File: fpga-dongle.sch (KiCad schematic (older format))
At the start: 109 parts, among them P1 USB_PWR, P2 PGM, P3 right, P4 left, P5 CONN_01X40, P6 CONN_01X40, P7 DBG_SWD, P8 USB_PWR, Q1 BC857, SW1 T1107A(6x3,8x2,5MM)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

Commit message: Add miltiple power source handling, reroute pertinent nets
Signed-off-by: Martin Ribelotta <martinribelotta@gmail.com>
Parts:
- added D10, D4, D5, D6, D7, D8, D9: 1N5819(S4SOD-123), Diodes_SMD:SOD-123, symbol D_Schottky
- added R42, R43, R44: 10k, Resistors_SMD:R_0805, symbol R
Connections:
- net +3V3: now also C3.2, U3.1 (Vin), U3.3 (EN), D4.1 (K), D5.1 (K), D6.1 (K); no longer C8.2, L1.2, P3.1 (P1), P4.1 (P1), U2.4 (Vout)
- net +5V: now also D10.1 (K), D7.1 (K), D8.1 (K), D9.1 (K); no longer C3.2, C5.2, C7.2, D1.1, F1.2, F2.2, U3.1 (Vin), U3.3 (EN)
- net GND: now also R44.1
- net CIAA_5V2: now reaches P3.2 (P2)
- net CIAA_5V2: now also D8.2 (A), R42.2
- net CIAA_5V1: now reaches P4.2 (P2)
- net CIAA_5V1: now also D7.2 (A)
- net at U6.45 (PIO0_17/CT32B0_C0/SCLK): now also R42.1, R43.1
- new net: C5.2, C7.2, D1.1, D9.2 (A), F1.2
- new net: C8.2, D4.2 (A), L1.2, U2.4 (Vout)
- new net: D10.2 (A), F2.2
- new net: R43.2, R44.2
- new net CIAA_3V3_1: D6.2 (A), P4.1 (P1)
- new net CIAA_3V3_2: D5.2 (A), P3.1 (P1)
- no-connect marks 39 -> 36
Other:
- moved on the sheet: PWRLED1, R9

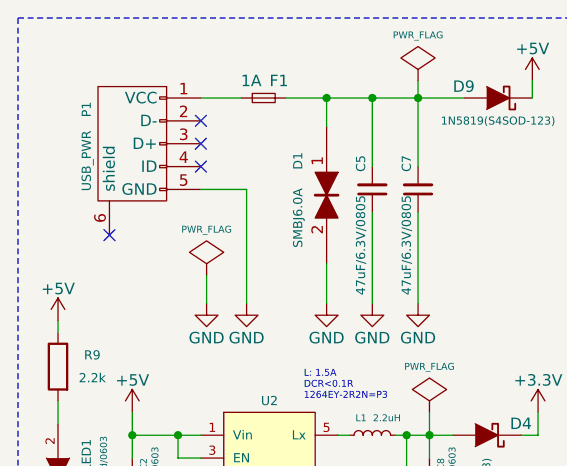
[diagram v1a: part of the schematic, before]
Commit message: Change USB power-only connector by screw connector
Signed-off-by: Martin Ribelotta <martinribelotta@gmail.com>
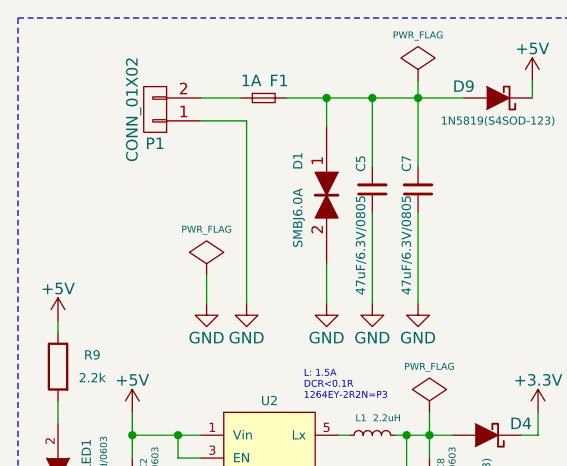
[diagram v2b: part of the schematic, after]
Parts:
- removed P1: USB_PWR, OLIMEX_Connectors-FP:USB_Mini-B-NOSILK, symbol USB_OTG
- added P1: CONN_01X02, Connect:AK300-2, symbol CONN_01X02
- D3: footprint LEDs:LED_0603 -> LEDs:LED_0805
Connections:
- net GND: now also P1.1 (P1)
- net at F1.1: now also P1.2 (P2)
- no-connect marks 36 -> 32
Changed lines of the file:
@@
 $EndComp
-$Comp
-L USB_OTG P1
-U 1 1 57D6B02D
-P 1450 1325
-F 0 "P1" H 1300 1525 40  0000 C CNN
-F 1 "USB_PWR" H 1525 1525 40  0000 C CNN
-F 2 "OLIMEX_Connectors-FP:USB_Mini-B-NOSILK" V 1400 1225 50  0001 C CNN
-F 3 "" V 1400 1225 50  0000 C CNN
-	1    1450 1325
-	0    -1   1    0
-$EndComp
-NoConn ~ 1350 1725
-NoConn ~ 1750 1425
 $Comp
 L TVS D1
@@
 F 0 "D3" H 11200 12575 50  0000 C CNN
 F 1 "LED" H 11200 12375 50  0000 C CNN
-F 2 "LEDs:LED_0603" H 11200 12475 50  0001 C CNN
+F 2 "LEDs:LED_0805" H 11200 12475 50  0001 C CNN
 F 3 "" H 11200 12475 50  0000 C CNN
 	1    11200 12475
@@
 Text Label 12225 13275 2    60   ~ 0
 USB_N
-NoConn ~ 1750 1225
-NoConn ~ 1750 1325
 Text Label 9850 13525 0    60   ~ 0
 D_USB_N
@@
 	1750 1125 1925 1125
 Wire Wire Line
-	1750 1525 1950 1525
-Wire Wire Line
-	1950 1525 1950 2025
+	1750 1225 1950 1225
+Wire Wire Line
+	1950 1225 1950 2025
 Wire Wire Line
 	2300 1250 2300 1125
@@
 Wire Wire Line
 	1125 2100 1125 2150
+$Comp
+L CONN_01X02 P1
+U 1 1 57F72785
+P 1550 1175
+F 0 "P1" H 1550 1325 50  0000 C CNN
+F 1 "CONN_01X02" V 1650 1175 50  0000 C CNN
+F 2 "Connect:AK300-2" H 1550 1175 50  0001 C CNN
+F 3 "" H 1550 1175 50  0000 C CNN
+	1    1550 1175
+	-1   0    0    1
+$EndComp
 $EndSCHEMATC

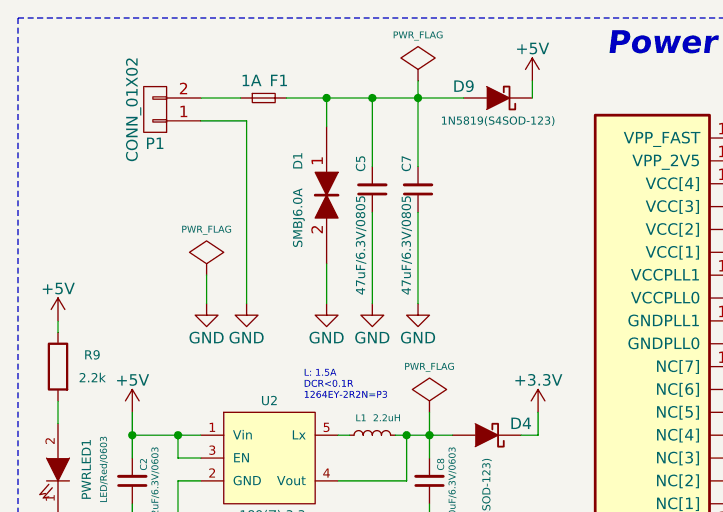
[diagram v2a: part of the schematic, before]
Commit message: Partial rework of changes lost in last conflict
Signed-off-by: Martin Ribelotta <martinribelotta@gmail.com>
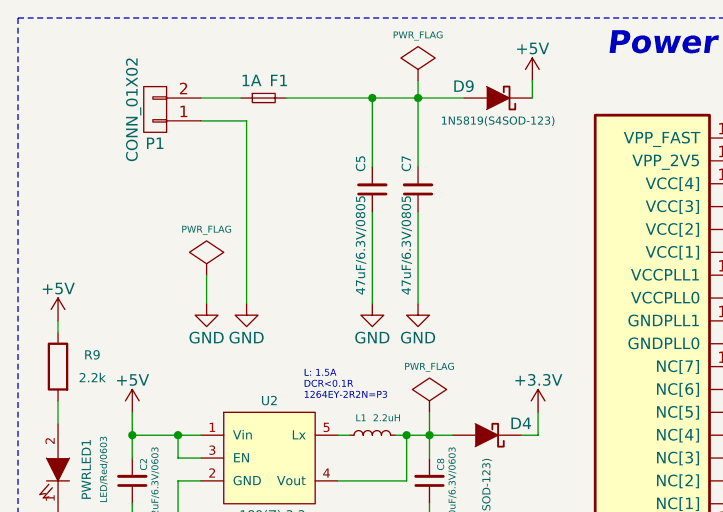
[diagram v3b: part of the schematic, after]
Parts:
- removed D1: SMBJ6.0A, Diodes_SMD:DO-214AB, symbol TVS
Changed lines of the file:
@@
 Power Supply
 $Comp
-L GND #PWR01
-U 1 1 579395D3
-P 2300 2025
-F 0 "#PWR01" H 2300 1775 50  0001 C CNN
-F 1 "GND" H 2300 1875 50  0000 C CNN
-F 2 "" H 2300 2025 60  0000 C CNN
-F 3 "" H 2300 2025 60  0000 C CNN
-	1    2300 2025
-	-1   0    0    -1
-$EndComp
-$Comp
 L C_Small C5
 U 1 1 579395D5
@@
 $EndComp
 $Comp
-L TVS D1
-U 1 1 57D6C6A1
-P 2300 1550
-F 0 "D1" H 2150 1425 40  0000 C CNN
-F 1 "SMBJ6.0A" H 2400 1425 40  0000 C CNN
-F 2 "Diodes_SMD:DO-214AB" H 2300 1550 50  0001 C CNN
-F 3 "" H 2300 1550 50  0000 C CNN
-	1    2300 1550
-	0    1    1    0
-$EndComp
-$Comp
 L L_Small L2
 U 1 1 57D707DC
@@
 	1950 1225 1950 2025
 Wire Wire Line
-	2300 1250 2300 1125
-Connection ~ 2300 1125
-Wire Wire Line
-	2300 2025 2300 1850
-Wire Wire Line
 	2950 3575 2950 3475

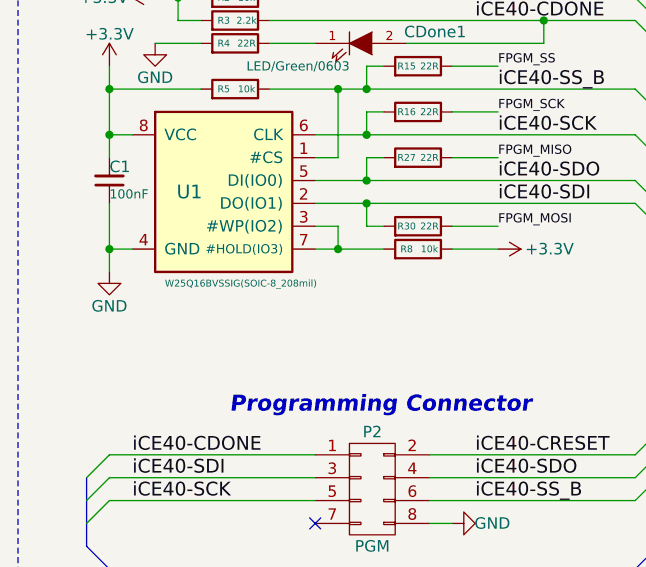
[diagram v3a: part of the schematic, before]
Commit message: More PCB annotations, some rework on GND plane
Signed-off-by: Martin Ribelotta <martinribelotta@gmail.com>
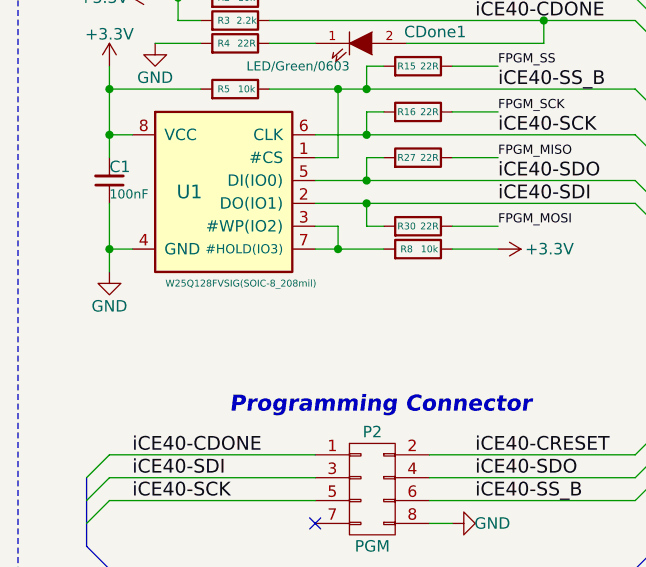
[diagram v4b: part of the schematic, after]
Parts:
- D3: footprint LEDs:LED_0805 -> LEDs:LED-0805
- U1: value W25Q16BVSSIG(SOIC-8_208mil) -> W25Q128FVSIG(SOIC-8_208mil)

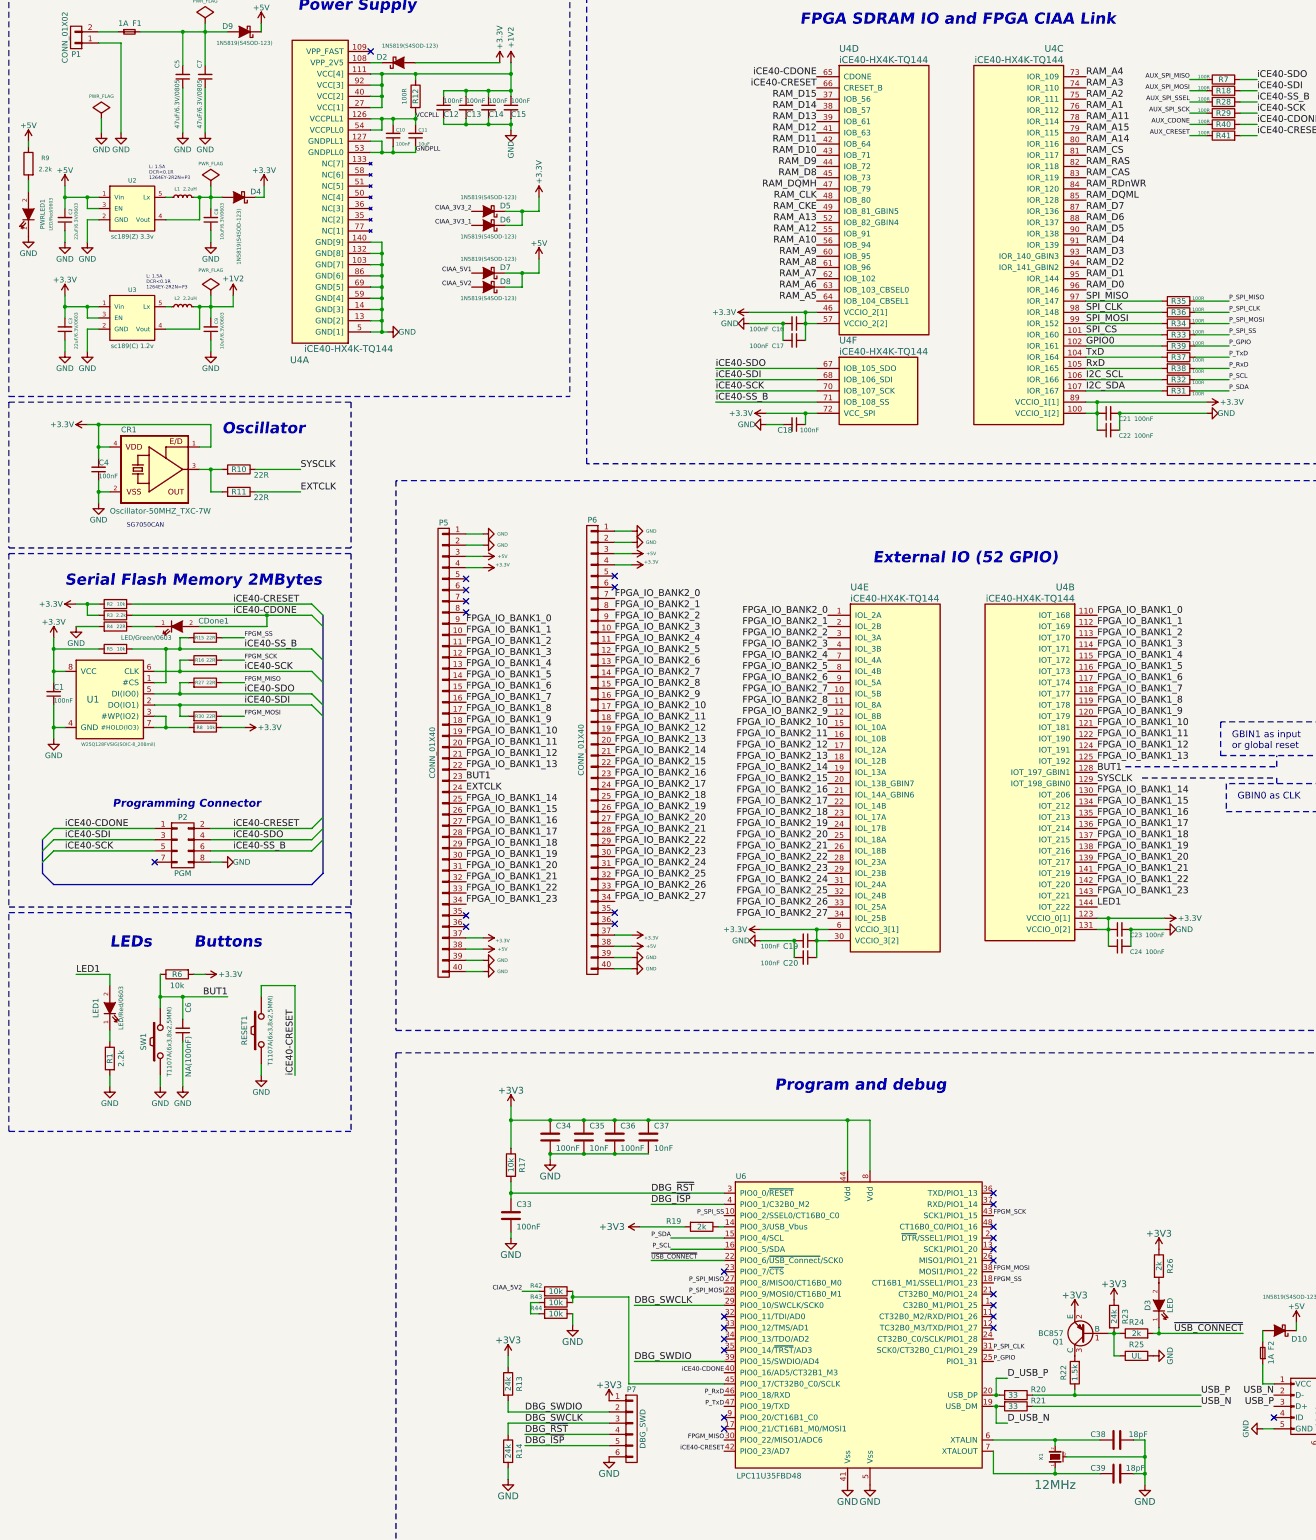
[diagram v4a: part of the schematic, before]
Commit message: Correct SDRAM footprint, add mounting joles, first gerber for cuotation
Signed-off-by: Martin Ribelotta <martinribelotta@gmail.com>
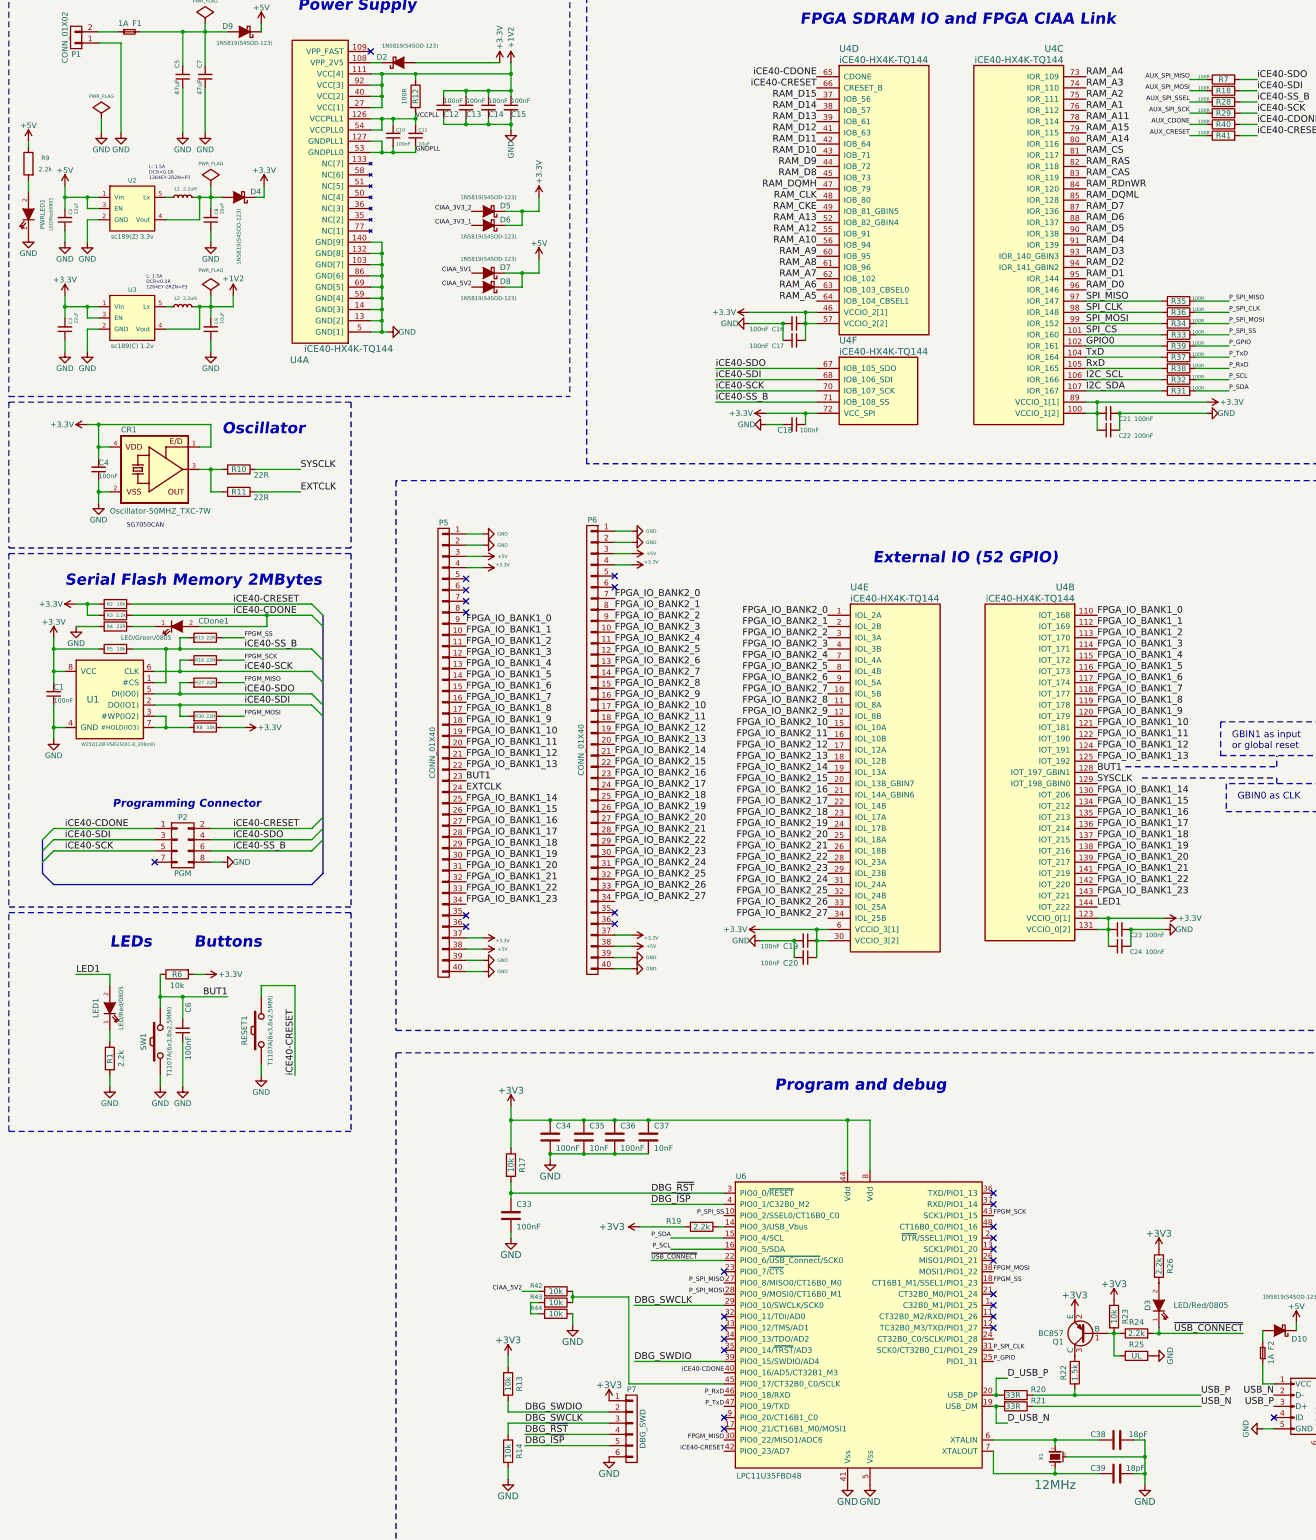
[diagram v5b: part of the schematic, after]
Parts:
- C2, C3: value 22uF/6.3V/0603 -> 22uF
- C5, C7: value 47uF/6.3V/0805 -> 47uF
- C6: value NA(100nF) -> 100nF
- C8, C9: value 10uF/6.3V/0603 -> 10uF
- CDone1: value LED/Green/0603 -> LED/Green/0805
- D3: value LED -> LED/Red/0805
- LED1, PWRLED1: value LED/Red/0603 -> LED/Red/0805
- R13, R14, R23: value 24k -> 10k
- R19, R24, R26: value 2k -> 2.2k
- R20, R21: value 33 -> 33R
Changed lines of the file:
@@
 P 2500 1525
 F 0 "C5" V 2550 1375 40  0000 L CNN
-F 1 "47uF/6.3V/0805" V 2550 1550 40  0000 L CNN
+F 1 "47uF" V 2550 1550 40  0000 L CNN
 F 2 "Capacitors_SMD:C_1206" H 2538 1375 30  0001 C CNN
 F 3 "" H 2500 1525 60  0000 C CNN
@@
 P 2700 1525
 F 0 "C7" V 2750 1375 40  0000 L CNN
-F 1 "47uF/6.3V/0805" V 2750 1550 40  0000 L CNN
+F 1 "47uF" V 2750 1550 40  0000 L CNN
 F 2 "Capacitors_SMD:C_1206" H 2738 1375 30  0001 C CNN
 F 3 "" H 2700 1525 60  0000 C CNN
@@
 P 1125 2750
 F 0 "PWRLED1" H 1125 2875 40  0000 C CNN
-F 1 "LED/Red/0603" H 1125 2950 30  0000 C CNN
+F 1 "LED/Red/0805" H 1125 2950 30  0000 C CNN
 F 2 "LEDs:LED-0805" H 1125 2750 60  0001 C CNN
 F 3 "" H 1125 2750 60  0000 C CNN
@@
 P 1450 2800
 F 0 "C2" V 1400 2700 30  0000 L CNN
-F 1 "22uF/6.3V/0603" V 1350 2650 30  0000 L CNN
+F 1 "22uF" V 1350 2650 30  0000 L CNN
 F 2 "Capacitors_SMD:C_1206" H 1488 2650 30  0001 C CNN
 F 3 "" H 1450 2800 60  0000 C CNN
@@
 P 2450 6425
 F 0 "CDone1" H 2775 6475 50  0000 C CNN
-F 1 "LED/Green/0603" H 2175 6325 40  0000 C CNN
+F 1 "LED/Green/0805" H 2175 6325 40  0000 C CNN
 F 2 "LEDs:LED-0805" H 2450 6425 60  0001 C CNN
 F 3 "" H 2450 6425 60  0000 C CNN
@@
 P 2500 10025
 F 0 "C6" V 2550 9775 50  0000 L CNN
-F 1 "NA(100nF)" V 2550 10075 50  0000 L CNN
+F 1 "100nF" V 2550 10075 50  0000 L CNN
 F 2 "Capacitors_SMD:C_0805" H 2538 9875 30  0001 C CNN
 F 3 "" H 2500 10025 60  0000 C CNN
@@
 P 1850 9825
 F 0 "LED1" H 1850 9950 50  0000 C CNN
-F 1 "LED/Red/0603" H 1850 9725 40  0000 C CNN
+F 1 "LED/Red/0805" H 1850 9725 40  0000 C CNN
 F 2 "LEDs:LED-0805" H 1850 9825 60  0001 C CNN
 F 3 "" H 1850 9825 60  0000 C CNN
@@
 P 2750 2800
 F 0 "C8" V 2700 2700 30  0000 L CNN
-F 1 "10uF/6.3V/0603" V 2650 2650 30  0000 L CNN
+F 1 "10uF" V 2650 2650 30  0000 L CNN
 F 2 "Capacitors_SMD:C_1206" H 2788 2650 30  0001 C CNN
 F 3 "" H 2750 2800 60  0000 C CNN
@@
 P 1450 3775
 F 0 "C3" V 1400 3675 30  0000 L CNN
-F 1 "22uF/6.3V/0603" V 1350 3625 30  0000 L CNN
+F 1 "22uF" V 1350 3625 30  0000 L CNN
 F 2 "Capacitors_SMD:C_1206" H 1488 3625 30  0001 C CNN
 F 3 "" H 1450 3775 60  0000 C CNN
@@
 P 2750 3775
 F 0 "C9" V 2700 3675 30  0000 L CNN
-F 1 "10uF/6.3V/0603" V 2650 3625 30  0000 L CNN
+F 1 "10uF" V 2650 3625 30  0000 L CNN
 F 2 "Capacitors_SMD:C_1206" H 2788 3625 30  0001 C CNN
 F 3 "" H 2750 3775 60  0000 C CNN
@@
 P 9925 13275
 F 0 "R20" V 9875 13475 50  0000 C CNN
-F 1 "33" V 9925 13250 50  0000 C CNN
+F 1 "33R" V 9925 13250 50  0000 C CNN
 F 2 "Resistors_SMD:R_0805" V 9855 13275 30  0001 C CNN
 F 3 "" H 9925 13275 30  0000 C CNN
@@
 P 9925 13375
 F 0 "R21" V 9875 13575 50  0000 C CNN
-F 1 "33" V 9925 13350 50  0000 C CNN
+F 1 "33R" V 9925 13350 50  0000 C CNN
 F 2 "Resistors_SMD:R_0805" V 9855 13375 30  0001 C CNN
 F 3 "" H 9925 13375 30  0000 C CNN
@@
 P 7125 11775
 F 0 "R19" V 7075 11525 50  0000 C CNN
-F 1 "2k" V 7125 11775 50  0000 C CNN
+F 1 "2.2k" V 7125 11775 50  0000 C CNN
 F 2 "Resistors_SMD:R_0805" V 7055 11775 30  0001 C CNN
 F 3 "" H 7125 11775 30  0000 C CNN
@@
 P 11000 12725
 F 0 "R24" V 11100 12725 50  0000 C CNN
-F 1 "2k" V 11000 12725 50  0000 C CNN
+F 1 "2.2k" V 11000 12725 50  0000 C CNN
 F 2 "Resistors_SMD:R_0805" V 10930 12725 30  0001 C CNN
 F 3 "" H 11000 12725 30  0000 C CNN
@@
 P 10800 12575
 F 0 "R23" V 10900 12575 50  0000 C CNN
-F 1 "24k" V 10800 12575 50  0000 C CNN
+F 1 "10k" V 10800 12575 50  0000 C CNN
 F 2 "Resistors_SMD:R_0805" V 10730 12575 30  0001 C CNN
 F 3 "" H 10800 12575 30  0000 C CNN
@@
 P 11200 12475
 F 0 "D3" H 11200 12575 50  0000 C CNN
-F 1 "LED" H 11200 12375 50  0000 C CNN
+F 1 "LED/Red/0805" V 11200 12100 50  0000 C CNN
 F 2 "LEDs:LED-0805" H 11200 12475 50  0001 C CNN
 F 3 "" H 11200 12475 50  0000 C CNN
@@
 P 11200 12125
 F 0 "R26" V 11300 12125 50  0000 C CNN
-F 1 "2k" V 11200 12125 50  0000 C CNN
+F 1 "2.2k" V 11200 12125 50  0000 C CNN
 F 2 "Resistors_SMD:R_0805" V 11130 12125 30  0001 C CNN
 F 3 "" H 11200 12125 30  0000 C CNN
@@
 P 5400 13175
 F 0 "R13" V 5500 13175 50  0000 C CNN
-F 1 "24k" V 5400 13175 50  0000 C CNN
+F 1 "10k" V 5400 13175 50  0000 C CNN
 F 2 "Resistors_SMD:R_0805" V 5330 13175 30  0001 C CNN
 F 3 "" H 5400 13175 30  0000 C CNN
@@
 P 5400 13775
 F 0 "R14" V 5500 13775 50  0000 C CNN
-F 1 "24k" V 5400 13775 50  0000 C CNN
+F 1 "10k" V 5400 13775 50  0000 C CNN
 F 2 "Resistors_SMD:R_0805" V 5330 13775 30  0001 C CNN
 F 3 "" H 5400 13775 30  0000 C CNN
@@
 P 11375 4325
 F 0 "R31" V 11375 4325 50  0000 C CNN
-F 1 "100R" V 11400 4500 30  0000 C CNN
+F 1 "100R" V 11350 4500 30  0000 C CNN
 F 2 "Resistors_SMD:R_0805" V 11305 4325 30  0001 C CNN
 F 3 "" H 11375 4325 30  0000 C CNN
@@
 P 11375 4225
 F 0 "R32" V 11375 4225 50  0000 C CNN
-F 1 "100R" V 11400 4400 30  0000 C CNN
+F 1 "100R" V 11350 4400 30  0000 C CNN
 F 2 "Resistors_SMD:R_0805" V 11305 4225 30  0001 C CNN
 F 3 "" H 11375 4225 30  0000 C CNN
@@
 P 11375 4025
 F 0 "R37" V 11375 4025 50  0000 C CNN
-F 1 "100R" V 11400 4200 30  0000 C CNN
+F 1 "100R" V 11350 4200 30  0000 C CNN
 F 2 "Resistors_SMD:R_0805" V 11305 4025 30  0001 C CNN
 F 3 "" H 11375 4025 30  0000 C CNN
@@
 P 11375 4125
 F 0 "R38" V 11375 4125 50  0000 C CNN
-F 1 "100R" V 11400 4300 30  0000 C CNN
+F 1 "100R" V 11350 4300 30  0000 C CNN
 F 2 "Resistors_SMD:R_0805" V 11305 4125 30  0001 C CNN
 F 3 "" H 11375 4125 30  0000 C CNN
